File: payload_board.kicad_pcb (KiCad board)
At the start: 4 copper layers, 100 x 100 mm, 100 parts, among them IC1 RP2040_QFN56, IC2 AZ1117CH-3.3TRG1, J1 Cam_PicoLock, J10 503398-1892, J12 FC Breakout, J15 SWC, J2 Cam_Conn, J3 Antenna_Conn, J4 usb jumper, J5 Display_Conn, J6 Breakout, J7 Molex_Micro_USB, J8 FC to EPS Connector, Q1 Q_PMOS_GSD, SW1 KMR2, SW2 KMR2, T13V TESTPOINTROUND1.5MMNO, T1V2 TESTPOINTROUND1.5MMNO, T3V3 TESTPOINTROUND1.5MMNO, U1 W25Q128JVPIQ TR, U2 MAX706RESA, U3 INA180A3, U4 INA180A3, U5 FAN5331SX, Y1 ABLS-12.000MHZ-B2-T

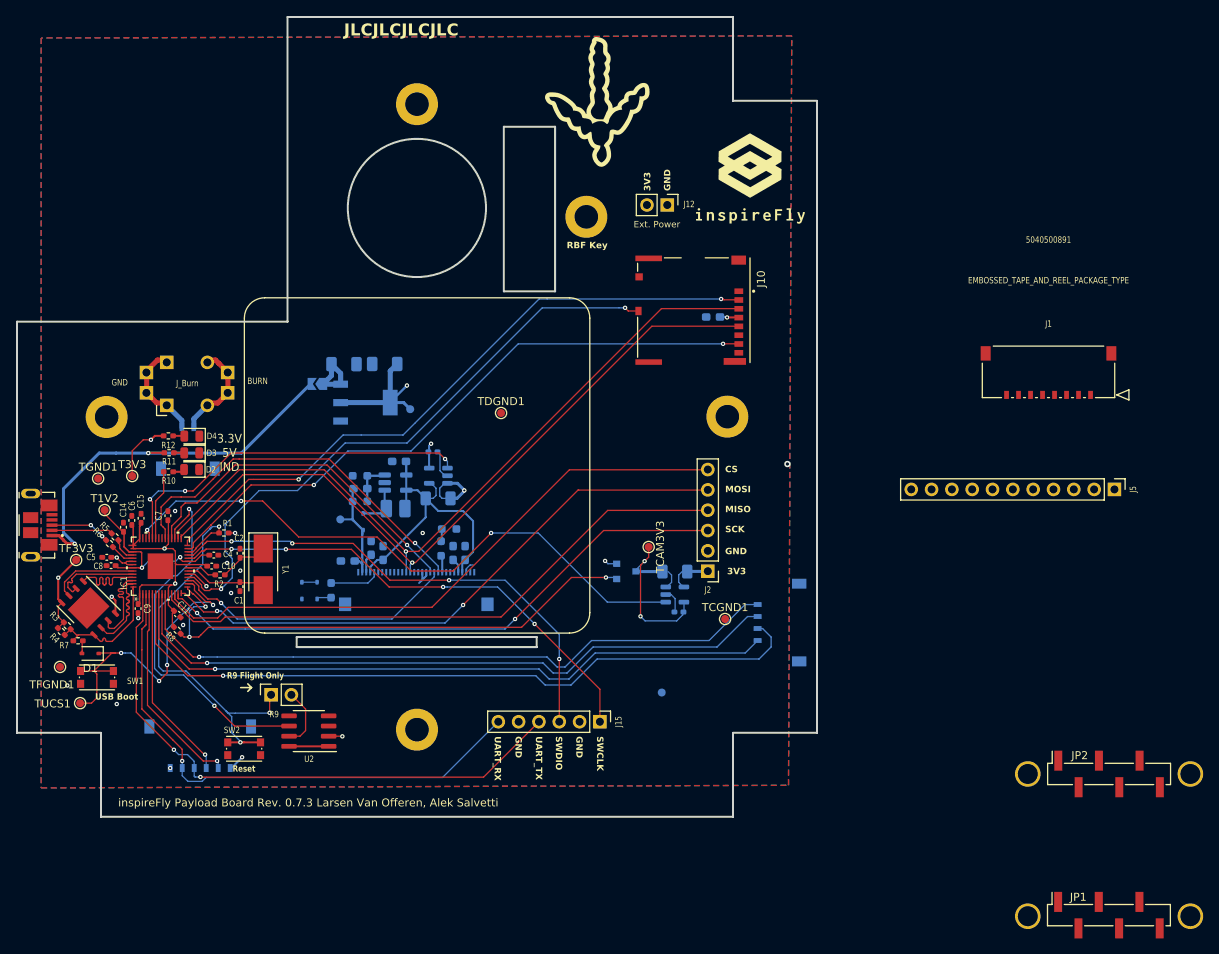
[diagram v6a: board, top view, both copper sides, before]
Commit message: Finalized part selection and gbr for 073 manufacturing.
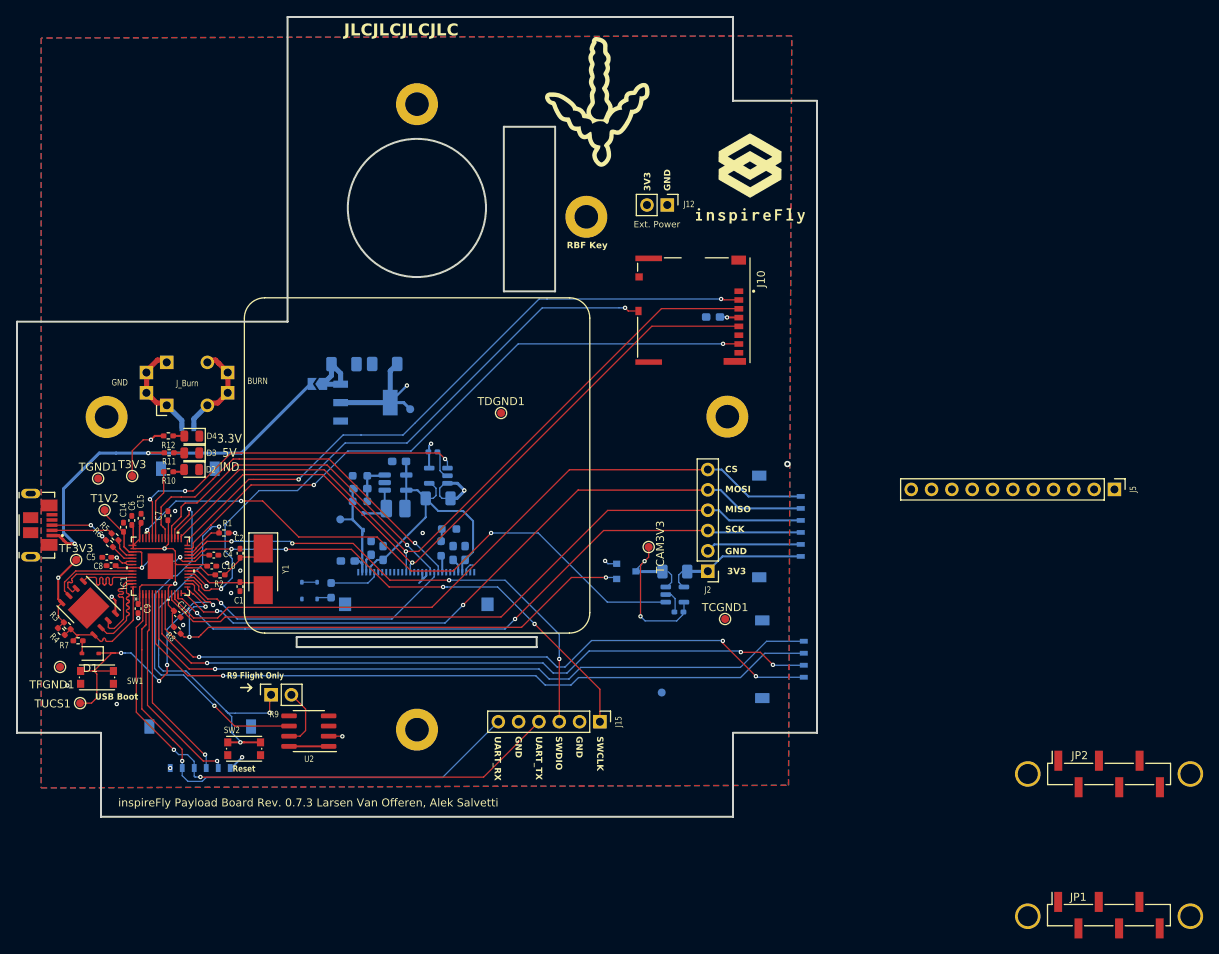
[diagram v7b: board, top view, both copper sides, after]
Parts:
- J1: footprint PayloadBoard:Molex_Pico_CON_5040500891 -> PayloadBoard:Molex_Pico_CON_5040500691; moved to B.Cu
- moved J1 41.5 mm to (111.0, 80.4), turned to -90 degrees
- moved J3 10.8 mm to (111.3, 95.5), turned to -90 degrees
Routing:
- net SPI1_CS_Cam: track 76.0 -> 89.0 mm
- net SPI1_MOSI_Cam: track 74.3 -> 87.1 mm
- net CIN-: track 4.66 -> 17.3 mm
- net SPI1_MISO_Cam: track 74.7 -> 87.1 mm
- net GND: track 16.4 -> 28.6 mm
- net SPI1_SCK_Cam: track 73.4 -> 85.4 mm
- net BURN_B: track 83.6 -> 89.6 mm, vias 1 -> 3
- net I2C1_SCL: track 84.6 -> 90.3 mm
- net BURN_A: track 84.4 -> 89.1 mm, vias 1 -> 3

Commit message: Flipped the outline and moved the screen and some of the connectors Now the front in Kicad is the back in the satelite (inside) and vice versa
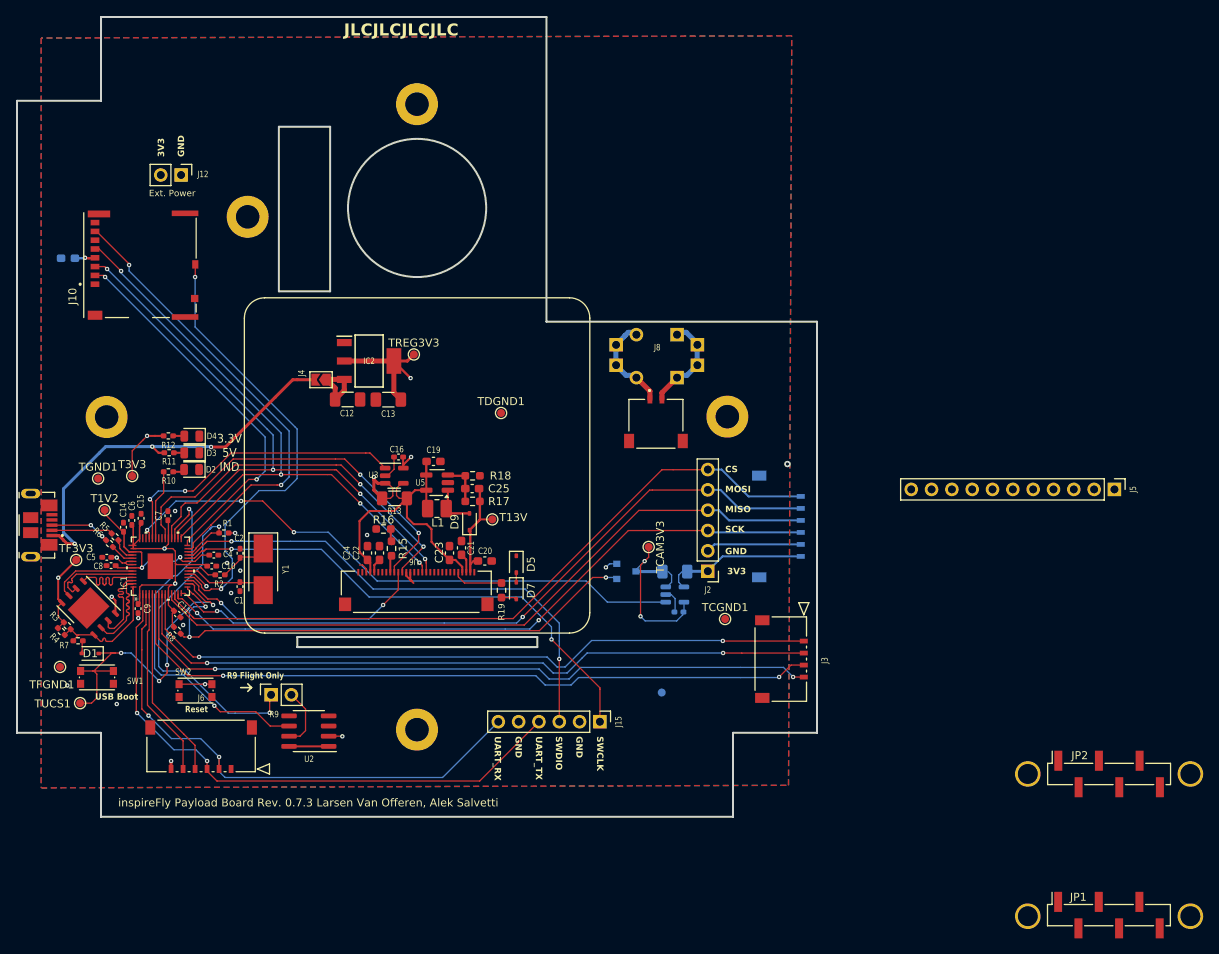
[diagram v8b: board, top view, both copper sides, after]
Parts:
- ?, G*** (x2), J_Burn: moved to B.Cu
- C12, C13, C16, C19, C20, C21, C22, C23, C24, C25, D5, D7, D9, IC2, J3, J4, J6, J8, L1, R13, R15, R16, R17, R18, R19, T13V, TREG3V3, U3, U5, U6: moved to F.Cu
- moved G*** 82.1 mm to (22.5, 33.8), turned to 180 degrees
- moved C18 81.0 mm to (19.4, 43.2)
- moved J_Burn 71.5 mm to (99.3, 60.3)
- moved J10 69.5 mm to (28.4, 44.0), turned to 90 degrees
- moved J12 60.9 mm to (33.5, 32.8)
- moved J8 58.6 mm to (92.9, 63.9), turned to 0 degrees
- moved G*** 46.9 mm to (38.8, 25.2), turned to 180 degrees
- moved ? 42.3 mm to (41.8, 38.0), turned to 180 degrees
- moved D5 27.0 mm to (75.4, 81.4), turned to -90 degrees
- moved D7 24.9 mm to (75.4, 84.7)
- moved R19 21.3 mm to (73.5, 84.7)
- moved T13V 19.0 mm to (72.4, 75.8), turned to 0 degrees
- moved C20 17.1 mm to (71.5, 81.0), turned to 180 degrees
- moved R17 14.1 mm to (69.9, 73.5), turned to 180 degrees
- moved R18 14.1 mm to (69.9, 70.3), turned to 0 degrees
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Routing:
- net SPI0_CS_SD: track 82.1 -> 47.8 mm
- net SPI0_MISO: track 79.9 -> 57.6 mm
- net SD_IND: track 77.2 -> 57.6 mm
- net SPI0_MOSI: track 93.7 -> 77.1 mm, vias 1 -> 4
- net SPI0_SCK: track 91.3 -> 77.2 mm, vias 1 -> 4
- net ADC0: track 45.9 -> 37.7 mm, vias 3 -> 2
- net ADC1: track 76.7 -> 72.8 mm
- net /~{RESET}: track 54.6 -> 50.7 mm
- net Disp_DC: track 35.9 -> 32.3 mm, vias 1 -> 2
- net Break_SDA: track 26.6 -> 23.9 mm, vias 1 -> 0
- net BURN_B: track 89.6 -> 87.6 mm, vias 3 -> 2
- net SPI0_CS_DISP: track 43.7 -> 45.5 mm, vias 1 -> 2
- net Disp_RST: track 47.6 -> 48.8 mm, vias 1 -> 2
- net +3.3V: track 97.0 -> 95.8 mm
- net SWCLK: track 63.2 -> 64.3 mm, vias 4 -> 2
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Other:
- outline, holes or cut-outs redrawn
